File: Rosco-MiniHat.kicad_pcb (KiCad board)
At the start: 4 copper layers, 73 x 42.5 mm, 9 parts, among them J6 Conn_01x05, U1 AS6C8008-55ZIN, U2 AS6C8008-55ZIN, U3 AS6C4008-55PCN, U4 AS6C4008-55PCN

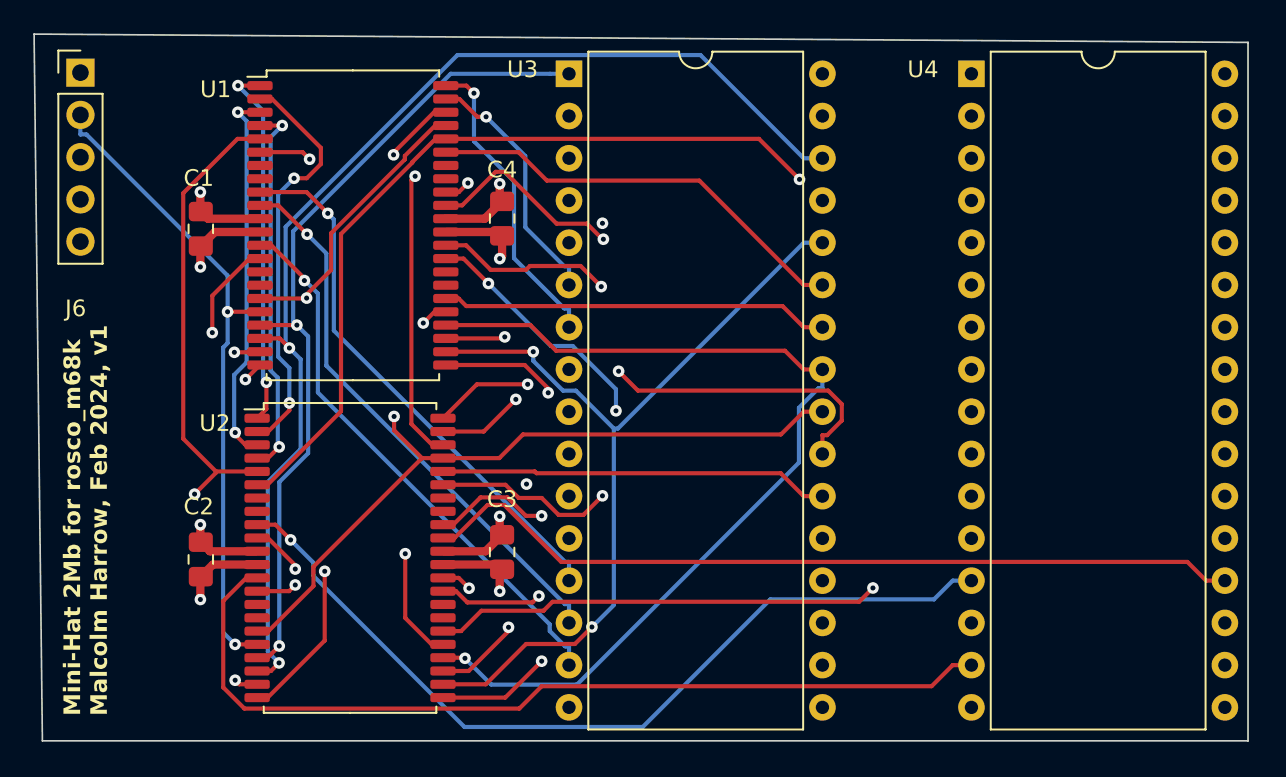
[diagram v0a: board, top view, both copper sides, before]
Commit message: Corrected RW/WR and CE2 connections as per advice on Discord
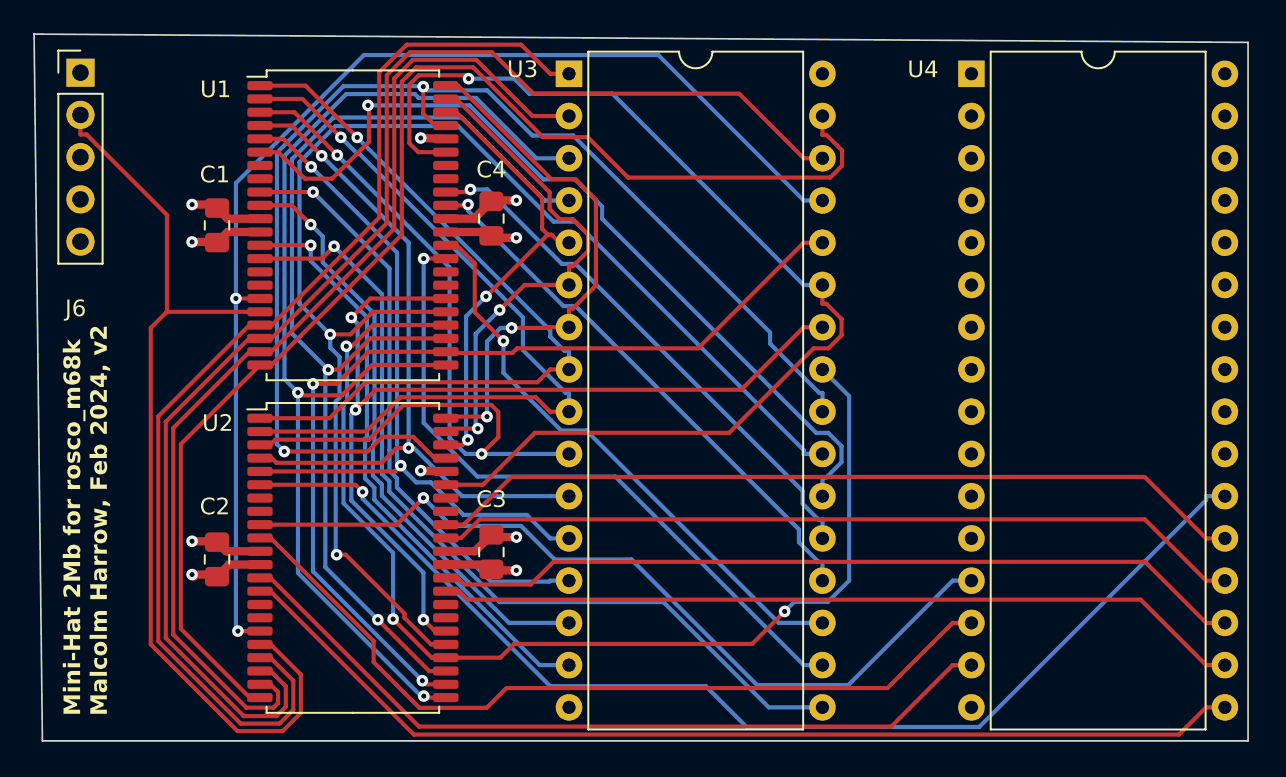
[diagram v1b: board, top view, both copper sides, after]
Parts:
- moved C1 1.00 mm to (66.5, 61.5)
- moved C2 0.97 mm to (66.5, 81.6)
- moved C3 0.64 mm to (83.0, 81.1)
- moved C4 0.64 mm to (83.0, 61.1)
- moved U2 0.17 mm to (74.7, 81.5)
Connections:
- U1 pad 17: WR -> RW
- U1 pad 40: EVENRAMSEL -> +5V
- U2 pad 17: WR -> RW
- U2 pad 40: ODDRAMSEL -> +5V
- U3 pad 29: unconnected-(U3-WE#-Pad29) -> RW
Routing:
- net +5V: track 132.4 -> 20.7 mm, vias 4 -> 6
- net GND: track 119.2 -> 18.4 mm
- net RW: track 0.00 -> 71.8 mm, vias 0 -> 2
- net A11: track 53.6 -> 81.8 mm, vias 3 -> 2
- net A13: track 36.4 -> 63.0 mm
- net ODDRAMSEL: track 72.3 -> 51.4 mm
- net A15: track 48.7 -> 67.4 mm
- net A20: track 39.4 -> 57.4 mm, vias 2 -> 0
- net A19: track 50.4 -> 68.2 mm, vias 2 -> 0
- net A1: track 57.1 -> 44.6 mm, vias 1 -> 2
- net EVENRAMSEL: track 82.0 -> 70.2 mm
- net A9: track 55.6 -> 67.4 mm
- net A18: track 70.4 -> 82.1 mm, vias 2 -> 0
- net D3: track 62.7 -> 52.3 mm
- net A12: track 57.7 -> 67.9 mm, vias 1 -> 3
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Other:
- board text added: "Mini-Hat 2Mb for rosco_m68k Malcolm Harrow, Feb 2024, v2"
- board text removed: "Mini-Hat 2Mb for rosco_m68k Malcolm Harrow, Feb 2024, v1"

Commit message: v3 with fix up to J6
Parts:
- C1, C2, C3, C4: value 100uF -> 100nF
- moved J6 0.42 mm to (58.6, 52.5)
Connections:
- J6 pad 1: EXPSEL -> A23
- J6 pad 2: A20 -> A22
- J6 pad 4: A22 -> A20
- J6 pad 5: A23 -> EXPSEL
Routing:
- net A20: track 57.4 -> 54.9 mm
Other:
- board size 73 x 42.5 mm -> 72.5 x 42.4 mm
- board text added: "Mini-Hat 2Mb for rosco_m68k Malcolm Harrow, Feb 2024, v3"
- board text removed: "Mini-Hat 2Mb for rosco_m68k Malcolm Harrow, Feb 2024, v2"
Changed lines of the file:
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@@
   (net 83 "unconnected-(U4-A15-Pad31)")
   (footprint "Connector_PinHeader_2.54mm:PinHeader_1x05_P2.54mm_Vertical" (layer "F.Cu")
-    (at 58.288 52.32)
+    (at 58.638 52.55)
     (descr "Through hole straight pin header, 1x05, 2.54mm pitch, single row")
     (tags "Through hole pin header THT 1x05 2.54mm single row")
@@
     (property "ki_keywords" "connector")
     (attr through_hole)
-    (fp_text reference "J6" (at -0.288 14.18) (layer "F.SilkS")
+    (fp_text reference "J6" (at -0.138 12.95) (layer "F.SilkS")
         (effects (font (size 1 1) (thickness 0.15)))
     )
@@
       (stroke (width 0.1) (type solid)) (layer "F.Fab"))
     (pad "1" thru_hole rect (at 0 0) (size 1.7 1.7) (drill 1) (layers "*.Cu" "*.Mask")
-      (net 3 "EXPSEL") (pinfunction "Pin_1") (pintype "passive+no_connect"))
+      (net 7 "A23") (pinfunction "Pin_1") (pintype "passive+no_connect"))
     (pad "2" thru_hole oval (at 0 2.54) (size 1.7 1.7) (drill 1) (layers "*.Cu" "*.Mask")
-      (net 4 "A20") (pinfunction "Pin_2") (pintype "passive"))
+      (net 6 "A22") (pinfunction "Pin_2") (pintype "passive+no_connect"))
     (pad "3" thru_hole oval (at 0 5.08) (size 1.7 1.7) (drill 1) (layers "*.Cu" "*.Mask")
       (net 5 "A21") (pinfunction "Pin_3") (pintype "passive+no_connect"))
     (pad "4" thru_hole oval (at 0 7.62) (size 1.7 1.7) (drill 1) (layers "*.Cu" "*.Mask")
-      (net 6 "A22") (pinfunction "Pin_4") (pintype "passive+no_connect"))
+      (net 4 "A20") (pinfunction "Pin_4") (pintype "passive"))
     (pad "5" thru_hole oval (at 0 10.16) (size 1.7 1.7) (drill 1) (layers "*.Cu" "*.Mask")
-      (net 7 "A23") (pinfunction "Pin_5") (pintype "passive+no_connect"))
+      (net 3 "EXPSEL") (pinfunction "Pin_5") (pintype "passive+no_connect"))
     (model "${KICAD6_3DMODEL_DIR}/Connector_PinHeader_2.54mm.3dshapes/PinHeader_1x05_P2.54mm_Vertical.wrl"
       (offset (xyz 0 0 0))
@@
         (effects (font (size 1 1) (thickness 0.15)))
     )
-    (fp_text value "100uF" (at 0 1.68 90) (layer "F.Fab")
+    (fp_text value "100nF" (at 0 1.68 90) (layer "F.Fab")
         (effects (font (size 1 1) (thickness 0.15)))
     )
@@
         (effects (font (size 1 1) (thickness 0.15)))
     )
-    (fp_text value "100uF" (at 0 1.68 90) (layer "F.Fab")
+    (fp_text value "100nF" (at 0 1.68 90) (layer "F.Fab")
         (effects (font (size 1 1) (thickness 0.15)))
     )
@@
         (effects (font (size 1 1) (thickness 0.15)))
     )
-    (fp_text value "100uF" (at 0 1.68 90) (layer "F.Fab")
+    (fp_text value "100nF" (at 0 1.68 90) (layer "F.Fab")
         (effects (font (size 1 1) (thickness 0.15)))
     )
@@
         (effects (font (size 1 1) (thickness 0.15)))
     )
-    (fp_text value "100uF" (at 0 1.68 90) (layer "F.Fab")
+    (fp_text value "100nF" (at 0 1.68 90) (layer "F.Fab")
         (effects (font (size 1 1) (thickness 0.15)))
     )
@@
     )
   )
-  (gr_line (start 128.5 50.5) (end 128.5 92.5)
+  (gr_line (start 128.75 92.65) (end 128.75 50.35)
     (stroke (width 0.1) (type default)) (layer "Edge.Cuts"))
-  (gr_line (start 128.5 92.5) (end 56 92.5)
+  (gr_line (start 128.75 50.35) (end 56.25 50.3)
     (stroke (width 0.1) (type default)) (layer "Edge.Cuts"))
-  (gr_line (start 56 92.5) (end 55.5 50)
+  (gr_line (start 56.25 92.6) (end 128.75 92.65)
     (stroke (width 0.1) (type default)) (layer "Edge.Cuts"))
-  (gr_line (start 55.5 50) (end 128.5 50.5)
+  (gr_line (start 56.25 50.3) (end 56.25 92.6)
     (stroke (width 0.1) (type default)) (layer "Edge.Cuts"))
-  (gr_text "Mini-Hat 2Mb for rosco_m68k\nMalcolm Harrow, Feb 2024, v2" (at 60 91 90) (layer "F.SilkS")
+  (gr_text "Mini-Hat 2Mb for rosco_m68k\nMalcolm Harrow, Feb 2024, v3" (at 60 91 90) (layer "F.SilkS")
     (effects (font (size 1 1) (thickness 0.25) bold) (justify left bottom))
   )
@@
   (via (at 65 82.5) (size 0.7) (drill 0.3) (layers "F.Cu" "B.Cu") (net 2))
   (via (at 65 62.5) (size 0.7) (drill 0.3) (layers "F.Cu" "B.Cu") (net 2))
-  (segment (start 63.4864 66.7) (end 63.4864 60.8695) (width 0.25) (layer "F.Cu") (net 4))
-  (segment (start 63.4864 60.8695) (end 58.6538 56.0369) (width 0.25) (layer "F.Cu") (net 4))
+  (segment (start 69.0825 66.7) (end 68.0645 66.7) (width 0.25) (layer "F.Cu") (net 4))
+  (segment (start 68.0645 66.7) (end 62.5145 72.25) (width 0.25) (layer "F.Cu") (net 4))
+  (segment (start 62.5145 72.25) (end 62.5145 86.6945) (width 0.25) (layer "F.Cu") (net 4))
   (segment (start 69.7268 86.7) (end 69.0825 86.7) (width 0.25) (layer "F.Cu") (net 4))
-  (segment (start 63.4864 66.7) (end 62.5145 67.6719) (width 0.25) (layer "F.Cu") (net 4))
-  (segment (start 62.5145 67.6719) (end 62.5145 86.6945) (width 0.25) (layer "F.Cu") (net 4))
   (segment (start 70.4472 91.9159) (end 71.5407 90.8224) (width 0.25) (layer "F.Cu") (net 4))
+  (segment (start 58.638 60.17) (end 62.5145 64.0465) (width 0.25) (layer "F.Cu") (net 4))
   (segment (start 67.7359 91.9159) (end 70.4472 91.9159) (width 0.25) (layer "F.Cu") (net 4))
   (segment (start 62.5145 86.6945) (end 67.7359 91.9159) (width 0.25) (layer "F.Cu") (net 4))
-  (segment (start 63.4864 66.7) (end 69.0825 66.7) (width 0.25) (layer "F.Cu") (net 4))
-  (segment (start 58.288 54.86) (end 58.288 56.0369) (width 0.25) (layer "F.Cu") (net 4))
-  (segment (start 58.6538 56.0369) (end 58.288 56.0369) (width 0.25) (layer "F.Cu") (net 4))
+  (segment (start 62.5145 72.25) (end 62.5145 64.0465) (width 0.25) (layer "F.Cu") (net 4))
+  (segment (start 58.638 60.87) (end 58.638 60.17) (width 0.25) (layer "F.Cu") (net 4))
   (segment (start 71.5407 90.8224) (end 71.5407 88.5139) (width 0.25) (layer "F.Cu") (net 4))
   (segment (start 71.5407 88.5139) (end 69.7268 86.7) (width 0.25) (layer "F.Cu") (net 4))
